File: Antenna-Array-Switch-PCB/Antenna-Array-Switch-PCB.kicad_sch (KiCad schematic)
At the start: 0 parts

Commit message: PCB: Draw LNA circuit
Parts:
- added C3: 1uF, symbol Device:C
- added C4: 10uF, symbol Device:C
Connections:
- new net +5V: C3.1, C4.1
- new net GNDA: C3.2, C4.2
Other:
- added sheet AntennaBranch (AntennaBranch.kicad_sch)
- added sheet AntennaBranch1 (AntennaBranch.kicad_sch)
- added sheet AntennaBranch2 (AntennaBranch.kicad_sch)
- added sheet Microcontroller (Microcontroller.kicad_sch)

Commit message: PCB: Assign footprints where sensible
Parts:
- C3: footprint (none) -> Capacitor_SMD:C_0603_1608Metric_Pad1.08x0.95mm_HandSolder
- C4: footprint (none) -> Capacitor_SMD:C_1206_3216Metric_Pad1.33x1.80mm_HandSolder
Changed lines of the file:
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@@
 			)
 		)
-		(property "Footprint" ""
+		(property "Footprint" "Capacitor_SMD:C_0603_1608Metric_Pad1.08x0.95mm_HandSolder"
 			(at 37.7952 161.29 0)
 			(hide yes)
@@
 			)
 		)
-		(property "Footprint" ""
+		(property "Footprint" "Capacitor_SMD:C_1206_3216Metric_Pad1.33x1.80mm_HandSolder"
 			(at 53.0352 161.29 0)
 			(hide yes)

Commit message: PCB: Add MCU, switch
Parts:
- added C24, C27: 100uF, Capacitor_SMD:C_1206_3216Metric_Pad1.33x1.80mm_HandSolder, symbol Device:C
- added C25, C26: 10uF, Capacitor_SMD:C_1206_3216Metric_Pad1.33x1.80mm_HandSolder, symbol Device:C
- added J4: Conn_SMA, Filter:Filter_1411-5_1.4x1.1mm, symbol Connector:Conn_Coaxial
- added NT1: NetTie_2, symbol Device:NetTie_2
- added U7: SKY13418-485LF, 00-project-footprints:Skyworks_QFN-14-1EP_2x2mm_SKY13418_Handsolder, symbol 00-project-symbols:SKY13418-485LF
- added U8: LM1117IMP-3.3, Package_TO_SOT_SMD:SOT-223-3_TabPin2, symbol Regulator_Linear:LM1117MP-3.3
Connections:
- net +5V: now also C24.1, C25.1, U8.3 (VI)
- net AntennaBranch/LNA_RF_OUTPUT: now also U7.3 (RF1)
- net AntennaBranch1/LNA_RF_OUTPUT: now also U7.9 (RF2)
- net AntennaBranch2/LNA_RF_OUTPUT: now also U7.2 (RF3)
- net GNDA: now also C24.2, C25.2, C26.2, C27.2, J4.2 (Ext), NT1.1, U7.EP (GND), U8.1 (GND)
- new net: J4.1 (In), U7.13 (ANT)
- new net +3.3V: C26.1, C27.1, U7.4 (VDD), U8.2 (VO)
- new net GNDD: NT1.2
- new net SWITCH_CTRL1_AT_1V8: U7.7 (CTRL1)
- new net SWITCH_CTRL2_AT_1V8: U7.6 (CTRL2)
- new net SWITCH_CTRL3_AT_1V8: U7.5 (CTRL3)
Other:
- note added: "Note: Get the wide temp. range "I" part. This is the regulated "analog 3v3"."
- note added: "TODO: Maybe use inductor."
- moved on the sheet: C4

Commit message: PCB: Assign footprints
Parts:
- NT1: footprint (none) -> NetTie:NetTie-2_SMD_Pad2.0mm
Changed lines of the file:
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@@
 			)
 		)
-		(property "Footprint" ""
+		(property "Footprint" "NetTie:NetTie-2_SMD_Pad2.0mm"
 			(at 99.06 176.53 0)
 			(hide yes)

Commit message: PCB: Layout an LNA segment
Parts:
- J4: footprint Filter:Filter_1411-5_1.4x1.1mm -> Connector_Coaxial:SMA_Amphenol_901-144_Vertical
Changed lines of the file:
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@@
 			)
 		)
-		(property "Footprint" "Filter:Filter_1411-5_1.4x1.1mm"
+		(property "Footprint" "Connector_Coaxial:SMA_Amphenol_901-144_Vertical"
 			(at 241.3 45.72 0)
 			(hide yes)

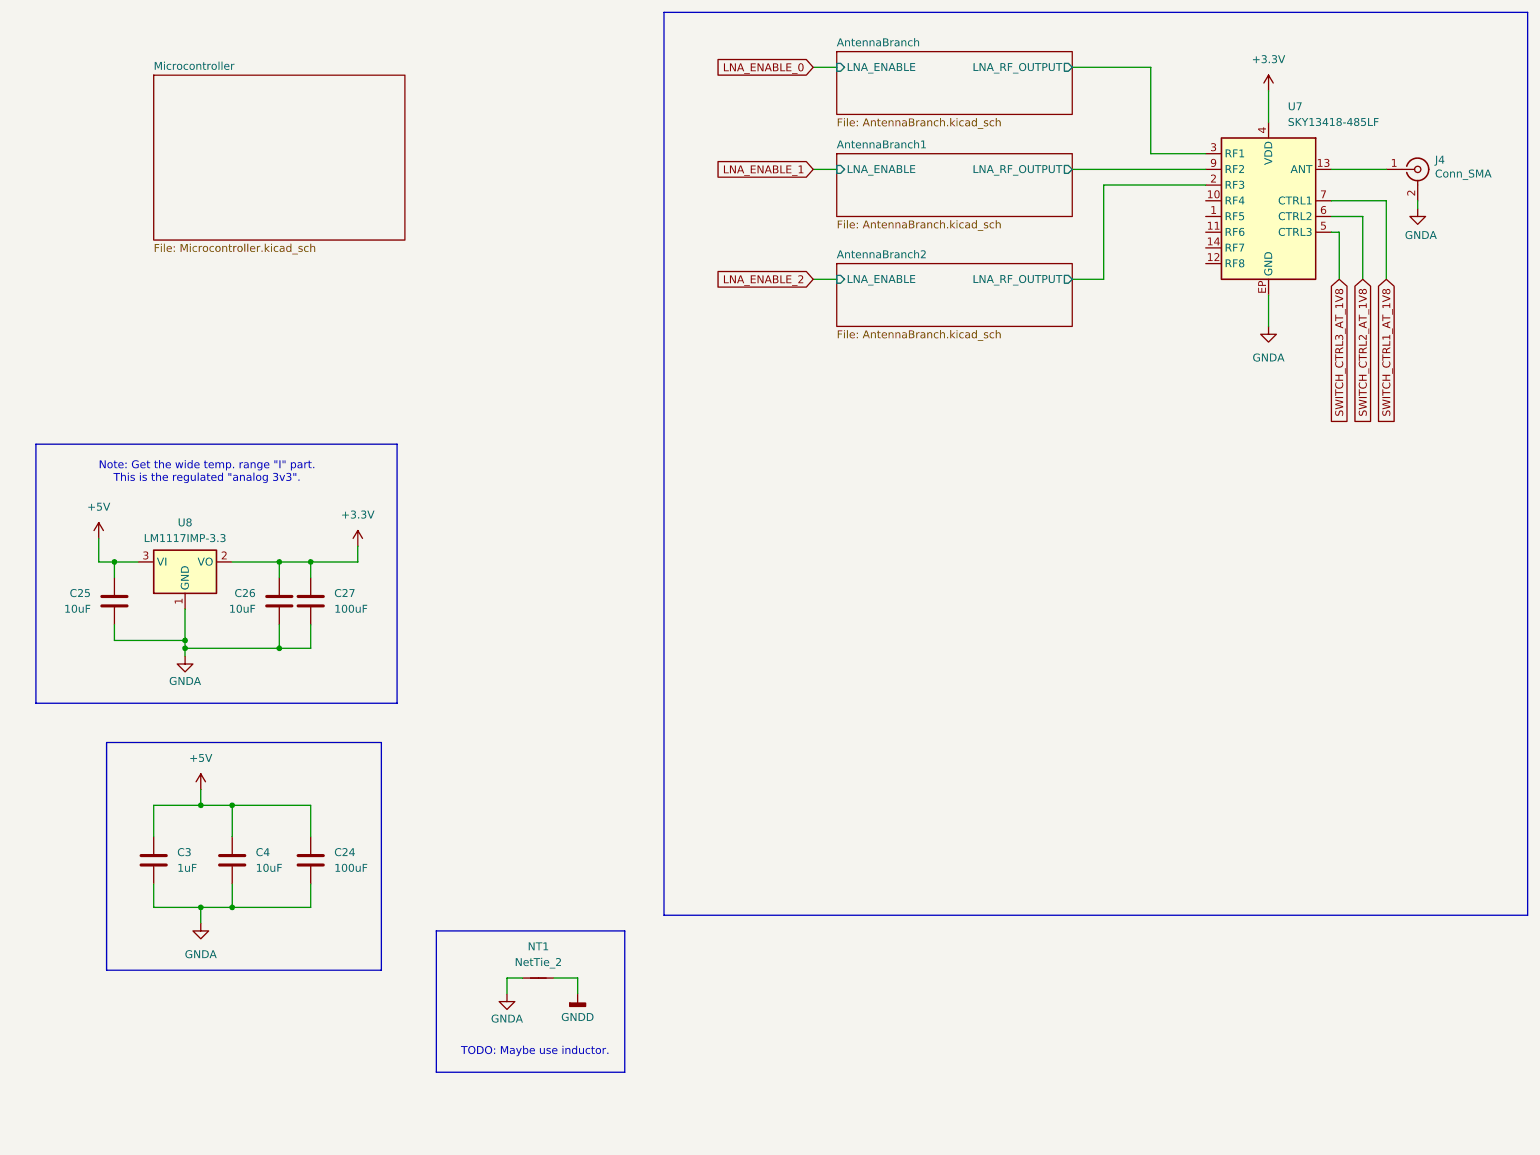
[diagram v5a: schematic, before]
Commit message: PCB, Docs: Layout, stackup, shielding
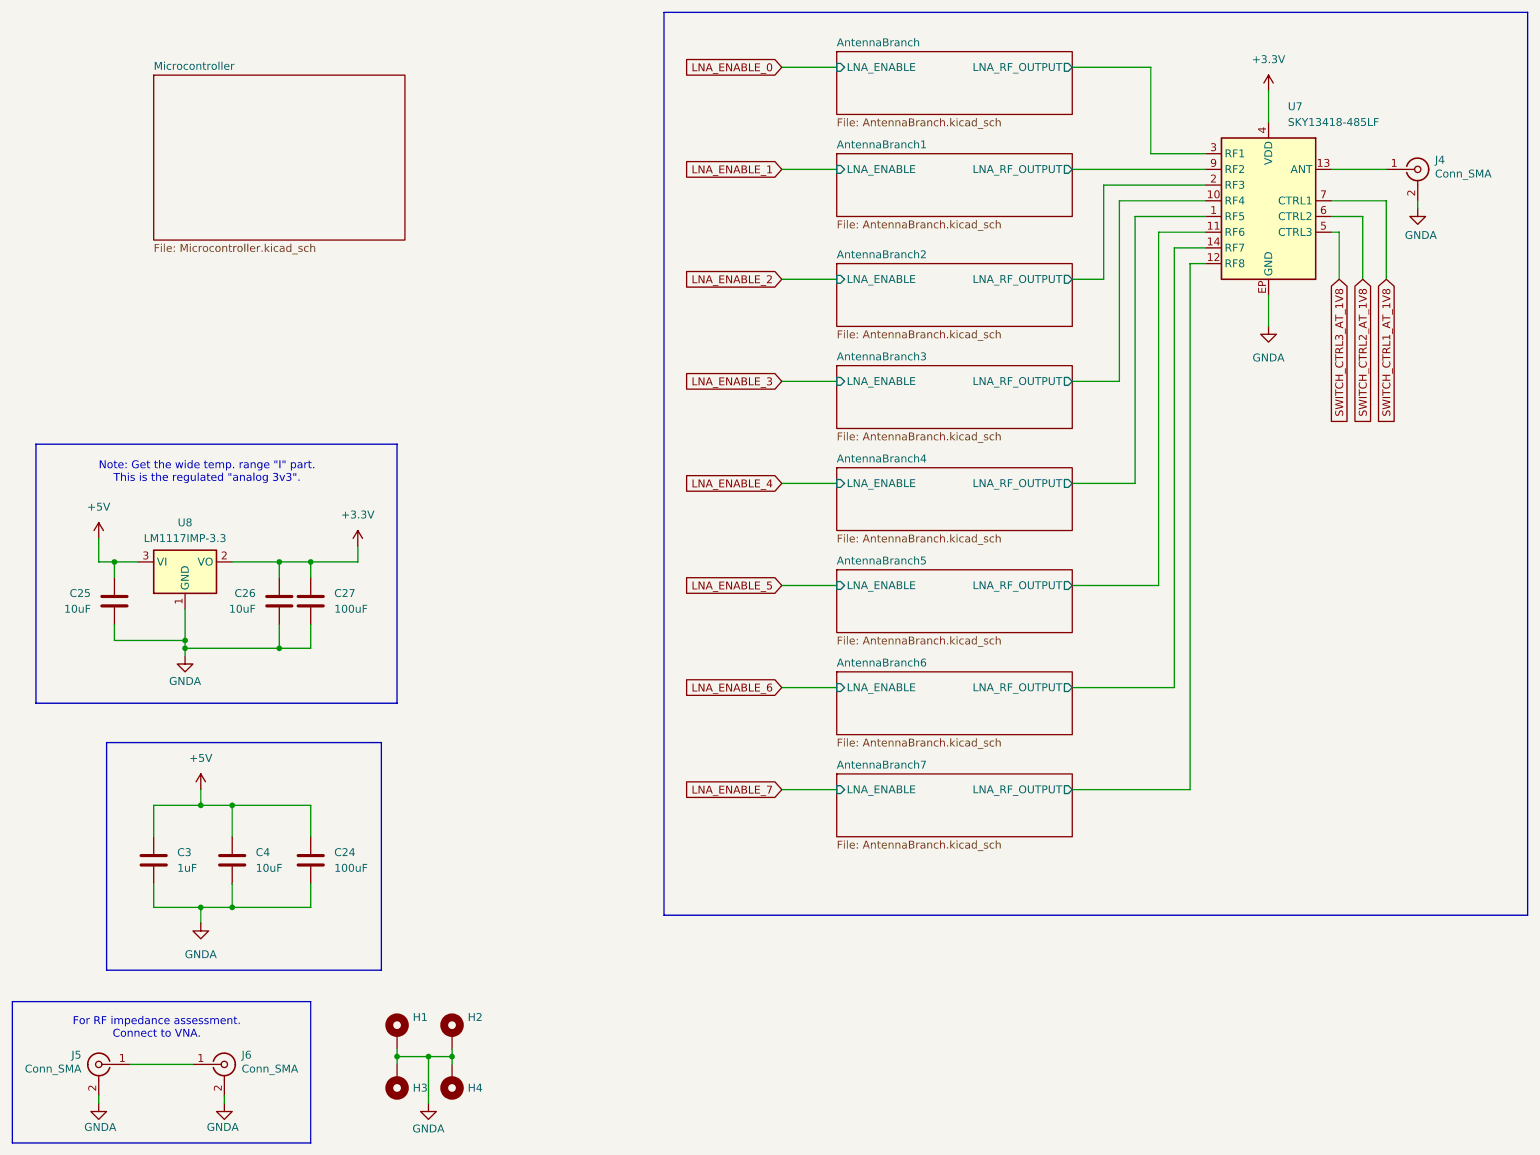
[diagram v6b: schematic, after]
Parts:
- removed NT1: NetTie_2, NetTie:NetTie-2_SMD_Pad2.0mm, symbol Device:NetTie_2
- added H1, H2, H3, H4: MountingHole_Pad, MountingHole:MountingHole_3.2mm_M3_Pad, symbol Mechanical:MountingHole_Pad
- added J5, J6: Conn_SMA, Connector_Coaxial:SMA_Amphenol_901-144_Vertical, symbol Connector:Conn_Coaxial
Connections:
- net GNDA: now also H1.1, H2.1, H3.1, H4.1, J5.2 (Ext), J6.2 (Ext)
- net AntennaBranch4/LNA_RF_OUTPUT: now reaches U7.1 (RF5)
- net AntennaBranch3/LNA_RF_OUTPUT: now reaches U7.10 (RF4)
- net AntennaBranch5/LNA_RF_OUTPUT: now reaches U7.11 (RF6)
- net AntennaBranch7/LNA_RF_OUTPUT: now reaches U7.12 (RF8)
- net AntennaBranch6/LNA_RF_OUTPUT: now reaches U7.14 (RF7)
- new net: J5.1 (In), J6.1 (In)
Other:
- added sheet AntennaBranch3 (AntennaBranch.kicad_sch)
- added sheet AntennaBranch4 (AntennaBranch.kicad_sch)
- added sheet AntennaBranch5 (AntennaBranch.kicad_sch)
- added sheet AntennaBranch6 (AntennaBranch.kicad_sch)
- added sheet AntennaBranch7 (AntennaBranch.kicad_sch)
- note added: "For RF impedance assessment. Connect to VNA."
- note removed: "TODO: Maybe use inductor."

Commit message: PCB: Layout - position connectors for autoplacement
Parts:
- added H5: MountingHole_Pad, MountingHole:MountingHole_3.2mm_M3_Pad, symbol Mechanical:MountingHole_Pad
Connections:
- net GNDA: now also H5.1
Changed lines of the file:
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@@
 	(wire
 		(pts
+			(xy 85.09 189.23) (xy 88.9 189.23)
+		)
+		(stroke
+			(width 0)
+			(type default)
+		)
+	)
+	(wire
+		(pts
 			(xy 49.53 148.59) (xy 44.45 148.59)
 		)
@@
 					(unit 1)
 				)
+			)
+		)
+	)
+	(symbol
+		(lib_id "Mechanical:MountingHole_Pad")
+		(at 91.44 189.23 270)
+		(unit 1)
+		(body_style 1)
+		(exclude_from_sim no)
+		(in_bom no)
+		(on_board yes)
+		(in_pos_files yes)
+		(dnp no)
+		(fields_autoplaced yes)
+		(property "Reference" "H5"
+			(at 95.25 189.2299 90)
+			(show_name no)
+			(do_not_autoplace no)
+			(effects
+				(font
+					(size 1.27 1.27)
+				)
+				(justify left)
+			)
+		)
+		(property "Value" "MountingHole_Pad"
+			(at 91.4401 191.77 0)
+			(hide yes)
+			(show_name no)
+			(do_not_autoplace no)
+			(effects
+				(font
+					(size 1.27 1.27)
+				)
+				(justify left)
+			)
+		)
+		(property "Footprint" "MountingHole:MountingHole_3.2mm_M3_Pad"
+			(at 91.44 189.23 0)
+			(hide yes)
+			(show_name no)
+			(do_not_autoplace no)
+			(effects
+				(font
+					(size 1.27 1.27)
+				)
+			)
+		)
+		(property "Datasheet" ""
+			(at 91.44 189.23 0)
+			(hide yes)
+			(show_name no)
+			(do_not_autoplace no)
+			(effects
+				(font
+					(size 1.27 1.27)
+				)
+			)
+		)
+		(property "Description" "Mounting Hole with connection"
+			(at 91.44 189.23 0)
+			(hide yes)
+			(show_name no)
+			(do_not_autoplace no)
+			(effects
+				(font
+					(size 1.27 1.27)
+				)
+			)
+		)
+		(pin "1"
+		)
+		(instances
+			(project "Antenna-Array-Switch-PCB"
+				(path "/53a2d682-f221-4d2b-9002-0fe959bb1f68"
+					(reference "H5")
+					(unit 1)
+				)

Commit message: PCB: Replicate layouts to all LNA chains
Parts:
- renumbered C25 to C101, C3 to C102, C4 to C103, C26 to C104, C27 to C105, C24 to C106, H1 to H101, H3 to H102, H2 to H103, H4 to H104, H5 to H105, J5 to J101, J6 to J102, J4 to J103, U8 to U101, U7 to U102
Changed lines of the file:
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@@
 		(in_pos_files yes)
 		(dnp no)
-		(property "Reference" "#PWR047"
+		(property "Reference" "#PWR0102"
 			(at 27.94 203.2 0)
 			(hide yes)
@@
 			(project "Antenna-Array-Switch-PCB"
 				(path "/53a2d682-f221-4d2b-9002-0fe959bb1f68"
-					(reference "#PWR047")
+					(reference "#PWR0102")
 					(unit 1)
 				)
@@
 		(dnp no)
 		(fields_autoplaced yes)
-		(property "Reference" "#PWR08"
+		(property "Reference" "#PWR0104"
 			(at 44.45 149.86 0)
 			(hide yes)
@@
 			(project "Antenna-Array-Switch-PCB"
 				(path "/53a2d682-f221-4d2b-9002-0fe959bb1f68"
-					(reference "#PWR08")
+					(reference "#PWR0104")
 					(unit 1)
 				)
@@
 		(dnp no)
 		(fields_autoplaced yes)
-		(property "Reference" "H3"
+		(property "Reference" "H102"
 			(at 78.74 194.3099 0)
 			(show_name no)
@@
 			(project "Antenna-Array-Switch-PCB"
 				(path "/53a2d682-f221-4d2b-9002-0fe959bb1f68"
-					(reference "H3")
+					(reference "H102")
 					(unit 1)
 				)
@@
 		(in_pos_files yes)
 		(dnp no)
-		(property "Reference" "C25"
+		(property "Reference" "C101"
 			(at 26.67 114.2999 0)
 			(show_name no)
@@
 			(project "Antenna-Array-Switch-PCB"
 				(path "/53a2d682-f221-4d2b-9002-0fe959bb1f68"
-					(reference "C25")
+					(reference "C101")
 					(unit 1)
 				)
@@
 		(dnp no)
 		(fields_autoplaced yes)
-		(property "Reference" "#PWR030"
+		(property "Reference" "#PWR0110"
 			(at 217.17 77.47 0)
 			(hide yes)
@@
 			(project "Antenna-Array-Switch-PCB"
 				(path "/53a2d682-f221-4d2b-9002-0fe959bb1f68"
-					(reference "#PWR030")
+					(reference "#PWR0110")
 					(unit 1)
 				)
@@
 		(dnp no)
 		(fields_autoplaced yes)
-		(property "Reference" "H2"
+		(property "Reference" "H103"
 			(at 87.63 182.8799 0)
 			(show_name no)
@@
 			(project "Antenna-Array-Switch-PCB"
 				(path "/53a2d682-f221-4d2b-9002-0fe959bb1f68"
-					(reference "H2")
+					(reference "H103")
 					(unit 1)
 				)
@@
 		(dnp no)
 		(fields_autoplaced yes)
-		(property "Reference" "C3"
+		(property "Reference" "C102"
 			(at 40.64 156.2099 0)
 			(show_name no)
@@
 			(project "Antenna-Array-Switch-PCB"
 				(path "/53a2d682-f221-4d2b-9002-0fe959bb1f68"
-					(reference "C3")
+					(reference "C102")
 					(unit 1)
 				)
@@
 		(dnp no)
 		(fields_autoplaced yes)
-		(property "Reference" "#PWR032"
+		(property "Reference" "#PWR0101"
 			(at 27.94 109.22 0)
 			(hide yes)
@@
 			(project "Antenna-Array-Switch-PCB"
 				(path "/53a2d682-f221-4d2b-9002-0fe959bb1f68"
-					(reference "#PWR032")
+					(reference "#PWR0101")
 					(unit 1)
 				)
@@
 		(dnp no)
 		(fields_autoplaced yes)
-		(property "Reference" "#PWR033"
+		(property "Reference" "#PWR0107"
 			(at 69.85 110.49 0)
 			(hide yes)
@@
 			(project "Antenna-Array-Switch-PCB"
 				(path "/53a2d682-f221-4d2b-9002-0fe959bb1f68"
-					(reference "#PWR033")
+					(reference "#PWR0107")
 					(unit 1)
 				)
@@
 		(in_pos_files yes)
 		(dnp no)
-		(property "Reference" "#PWR031"
+		(property "Reference" "#PWR0103"
 			(at 41.91 130.81 0)
 			(hide yes)
@@
 			(project "Antenna-Array-Switch-PCB"
 				(path "/53a2d682-f221-4d2b-9002-0fe959bb1f68"
-					(reference "#PWR031")
+					(reference "#PWR0103")
 					(unit 1)
 				)
@@
 		(dnp no)
 		(fields_autoplaced yes)
-		(property "Reference" "#PWR034"
+		(property "Reference" "#PWR0109"
 			(at 217.17 36.83 0)
 			(hide yes)
@@
 			(project "Antenna-Array-Switch-PCB"
 				(path "/53a2d682-f221-4d2b-9002-0fe959bb1f68"
-					(reference "#PWR034")
+					(reference "#PWR0109")
 					(unit 1)
 				)
@@
 		(in_pos_files yes)
 		(dnp no)
-		(property "Reference" "J6"
+		(property "Reference" "J102"
 			(at 51.054 188.976 0)
 			(show_name no)
@@
 			(project "Antenna-Array-Switch-PCB"
 				(path "/53a2d682-f221-4d2b-9002-0fe959bb1f68"
-					(reference "J6")
+					(reference "J102")
 					(unit 1)
 				)
@@
 		(in_pos_files yes)
 		(dnp no)
-		(property "Reference" "#PWR093"
+		(property "Reference" "#PWR0108"
 			(at 81.28 203.2 0)
 			(hide yes)
@@
 			(project "Antenna-Array-Switch-PCB"
 				(path "/53a2d682-f221-4d2b-9002-0fe959bb1f68"
-					(reference "#PWR093")
+					(reference "#PWR0108")
 					(unit 1)
 				)
@@
 		(in_pos_files yes)
 		(dnp no)
-		(property "Reference" "#PWR035"
+		(property "Reference" "#PWR0111"
 			(at 241.3 58.42 0)
 			(hide yes)
@@
 			(project "Antenna-Array-Switch-PCB"
 				(path "/53a2d682-f221-4d2b-9002-0fe959bb1f68"
-					(reference "#PWR035")
+					(reference "#PWR0111")
 					(unit 1)
 				)
@@
 		(in_pos_files yes)
 		(dnp no)
-		(property "Reference" "#PWR048"
+		(property "Reference" "#PWR0106"
 			(at 48.26 203.2 0)
 			(hide yes)
@@
 			(project "Antenna-Array-Switch-PCB"
 				(path "/53a2d682-f221-4d2b-9002-0fe959bb1f68"
-					(reference "#PWR048")
+					(reference "#PWR0106")
 					(unit 1)
 				)
@@
 		(in_pos_files yes)
 		(dnp no)
-		(property "Reference" "C26"
+		(property "Reference" "C104"
 			(at 53.34 114.2999 0)
 			(show_name no)
@@
 			(project "Antenna-Array-Switch-PCB"
 				(path "/53a2d682-f221-4d2b-9002-0fe959bb1f68"
-					(reference "C26")
+					(reference "C104")
 					(unit 1)
 				)
@@
 		(dnp no)
 		(fields_autoplaced yes)
-		(property "Reference" "H4"
+		(property "Reference" "H104"
 			(at 87.63 194.3099 0)
 			(show_name no)
@@
 			(project "Antenna-Array-Switch-PCB"
 				(path "/53a2d682-f221-4d2b-9002-0fe959bb1f68"
-					(reference "H4")
+					(reference "H104")
 					(unit 1)
 				)
@@
 		(dnp no)
 		(fields_autoplaced yes)
-		(property "Reference" "C24"
+		(property "Reference" "C106"
 			(at 66.04 156.2099 0)
 			(show_name no)
@@
 			(project "Antenna-Array-Switch-PCB"
 				(path "/53a2d682-f221-4d2b-9002-0fe959bb1f68"
-					(reference "C24")
+					(reference "C106")
 					(unit 1)
 				)
@@
 		(dnp no)
 		(fields_autoplaced yes)
-		(property "Reference" "U8"
+		(property "Reference" "U101"
 			(at 41.91 102.87 0)
 			(show_name no)
@@
 			(project "Antenna-Array-Switch-PCB"
 				(path "/53a2d682-f221-4d2b-9002-0fe959bb1f68"
-					(reference "U8")
+					(reference "U101")
 					(unit 1)
 				)
@@
 		(dnp no)
 		(fields_autoplaced yes)
-		(property "Reference" "U7"
+		(property "Reference" "U102"
 			(at 220.2881 35.56 0)
 			(show_name no)
@@
 			(project "Antenna-Array-Switch-PCB"
 				(path "/53a2d682-f221-4d2b-9002-0fe959bb1f68"
-					(reference "U7")
+					(reference "U102")
 					(unit 1)
 				)
@@
 		(in_pos_files yes)
 		(dnp no)
-		(property "Reference" "J5"
+		(property "Reference" "J101"
 			(at 25.146 188.976 0)
 			(show_name no)
@@
 			(project "Antenna-Array-Switch-PCB"
 				(path "/53a2d682-f221-4d2b-9002-0fe959bb1f68"
-					(reference "J5")
+					(reference "J101")
 					(unit 1)
 				)
@@
 		(dnp no)
 		(fields_autoplaced yes)
-		(property "Reference" "C4"
+		(property "Reference" "C103"
 			(at 53.34 156.2099 0)
 			(show_name no)
@@
 			(project "Antenna-Array-Switch-PCB"
 				(path "/53a2d682-f221-4d2b-9002-0fe959bb1f68"
-					(reference "C4")
+					(reference "C103")
 					(unit 1)
 				)
@@
 		(dnp no)
 		(fields_autoplaced yes)
-		(property "Reference" "#PWR07"
+		(property "Reference" "#PWR0105"
 			(at 44.45 173.99 0)
 			(hide yes)
@@
 			(project "Antenna-Array-Switch-PCB"
 				(path "/53a2d682-f221-4d2b-9002-0fe959bb1f68"
-					(reference "#PWR07")
+					(reference "#PWR0105")
 					(unit 1)
 				)
@@
 		(in_pos_files yes)
 		(dnp no)
-		(property "Reference" "J4"
+		(property "Reference" "J103"
 			(at 244.094 44.196 0)
 			(show_name no)
@@
 			(project "Antenna-Array-Switch-PCB"
 				(path "/53a2d682-f221-4d2b-9002-0fe959bb1f68"
-					(reference "J4")
+					(reference "J103")
 					(unit 1)
 				)
@@
 		(dnp no)
 		(fields_autoplaced yes)
-		(property "Reference" "H1"
+		(property "Reference" "H101"
 			(at 78.74 182.8799 0)
 			(show_name no)
@@
 			(project "Antenna-Array-Switch-PCB"
 				(path "/53a2d682-f221-4d2b-9002-0fe959bb1f68"
-					(reference "H1")
+					(reference "H101")
 					(unit 1)
 				)
@@
 		(in_pos_files yes)
 		(dnp no)
-		(property "Reference" "C27"
+		(property "Reference" "C105"
 			(at 66.04 114.2999 0)
 			(show_name no)
@@
 			(project "Antenna-Array-Switch-PCB"
 				(path "/53a2d682-f221-4d2b-9002-0fe959bb1f68"
-					(reference "C27")
+					(reference "C105")
 					(unit 1)
 				)
@@
 		(dnp no)
 		(fields_autoplaced yes)
-		(property "Reference" "H5"
+		(property "Reference" "H105"
 			(at 95.25 189.2299 90)
 			(show_name no)
@@
 			(project "Antenna-Array-Switch-PCB"
 				(path "/53a2d682-f221-4d2b-9002-0fe959bb1f68"
-					(reference "H5")
-					(unit 1)
-				)
+					(reference "H105")
+					(unit 1)
+				)
